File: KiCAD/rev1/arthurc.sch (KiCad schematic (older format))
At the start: 47 parts, among them IC1 ATMEGA328, P1 I/O, P10 CD2, P11 CD2, P12 CD1, P13 CD1, P14 I/O, P15 I/O, P16 I/O, P2 BAT, P4 CONN_6, P5 CONN_6, P6 LiPo, P7 GPS, P8 FTDI, P9 ISP, SW1 SW_PUSH, U1 3V3, X1 8MHz

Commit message: ArthurC rev1 (FTDI ver) complete.
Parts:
- X1: footprint ArthurC Lib:Xtal_SMD3 -> ArthurC Lib:Xtal_SMD4
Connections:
- net AREF: now reaches B1.1, IC1.20 (AREF)
- net A7: now reaches B8.1, IC1.22 (ADC7)
- net PC1 renamed A1
- net PC2 renamed A2
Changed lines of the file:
@@
 EN
 Text Label 3450 2350 0    40   ~ 0
-PC1
+A1
 Text Label 3450 2450 0    40   ~ 0
-PC2
+A2
 Text Label 3450 2550 0    40   ~ 0
 Ir_Dat
@@
 F 0 "X1" V 975 3300 60  0000 C CNN
 F 1 "8MHz" V 875 3375 60  0000 C CNN
-F 2 "ArthurC Lib:Xtal_SMD3" H 900 3050 60  0001 C CNN
+F 2 "ArthurC Lib:Xtal_SMD4" H 900 3050 60  0001 C CNN
 F 3 "" H 900 3050 60  0000 C CNN
 	1    900  3050
@@
 	10925 2400 10925 2350
 Connection ~ 10600 2400
+Text Label 3450 2950 0    50   ~ 0
+A7
+Text Label 1450 1700 0    50   ~ 0
+AREF
 $EndSCHEMATC

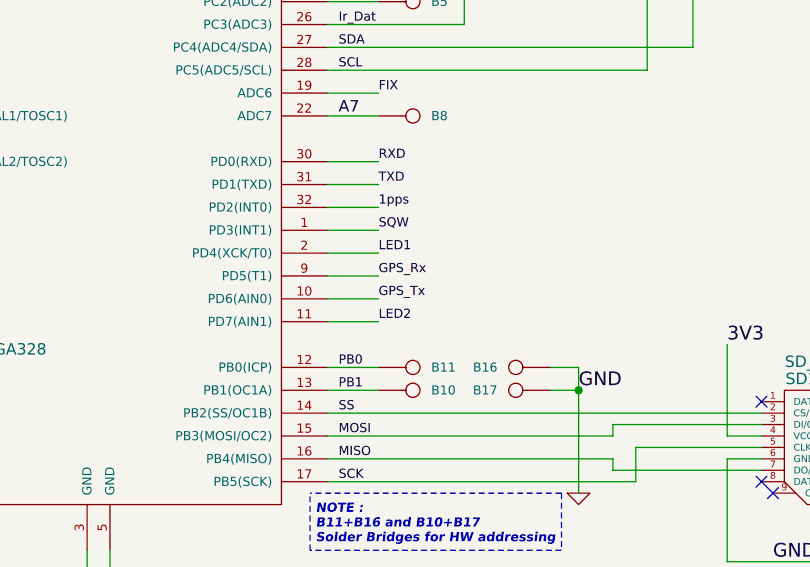
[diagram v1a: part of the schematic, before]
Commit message: ArthurC rev1 ready. Added LED breakout pads
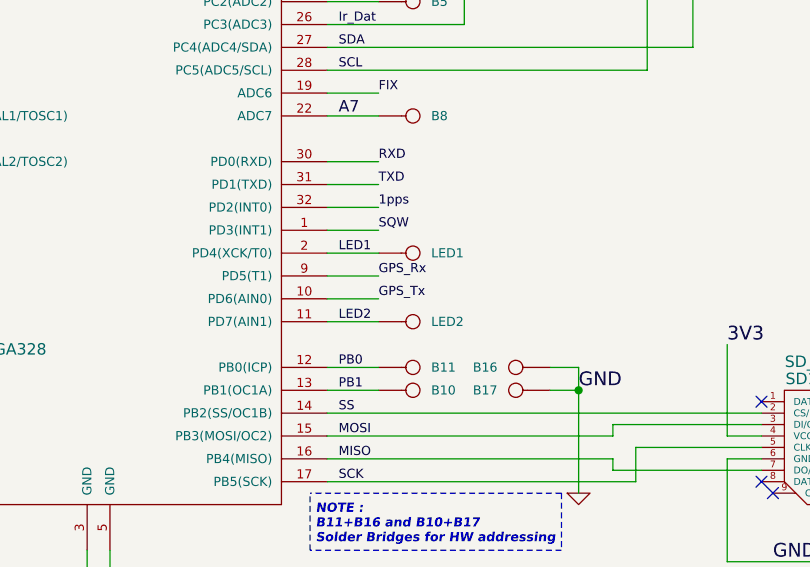
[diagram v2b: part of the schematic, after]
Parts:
- added LED1, LED2: I/O, ArthurC Lib:I%2fO, symbol I/O
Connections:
- net LED1: now also LED1.1
- net LED2: now also LED2.1
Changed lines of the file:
@@
 Text Label 3625 3350 0    40   ~ 0
 1pps
-Text Label 3625 3850 0    40   ~ 0
+Text Label 3450 3850 0    40   ~ 0
 LED2
-Text Label 3625 3550 0    40   ~ 0
+Text Label 3450 3550 0    40   ~ 0
 LED1
 Text Label 10025 2400 0    60   ~ 0
@@
 Text Label 1450 1700 0    50   ~ 0
 AREF
+$Comp
+L I/O LED1
+U 1 1 538094E5
+P 3775 3550
+F 0 "LED1" H 3855 3550 40  0000 L CNN
+F 1 "I/O" H 3775 3605 30  0001 C CNN
+F 2 "ArthurC Lib:I%2fO" H 3775 3550 60  0001 C CNN
+F 3 "" H 3775 3550 60  0001 C CNN
+	1    3775 3550
+	1    0    0    -1
+$EndComp
+$Comp
+L I/O LED2
+U 1 1 53809775
+P 3775 3850
+F 0 "LED2" H 3855 3850 40  0000 L CNN
+F 1 "I/O" H 3775 3905 30  0001 C CNN
+F 2 "ArthurC Lib:I%2fO" H 3775 3850 60  0001 C CNN
+F 3 "" H 3775 3850 60  0001 C CNN
+	1    3775 3850
+	1    0    0    -1
+$EndComp
 $EndSCHEMATC
